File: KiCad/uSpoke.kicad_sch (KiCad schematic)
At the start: 82 parts, among them J1 B2B-PH-K-S, J12 Amphenol 132289, J2 BAT+, J3 BAT-, J5 USB+, J6 USB-, J8 PLS-1x6, J9 PLS-1x3, Q2 AO3407A, Q3 AO3400, U2 TP4056, U4 LM3671MF-3.3, U6 STM32F103C8T6, X1 8MHz

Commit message: Rename to uSpoke
(cherry picked from commit a0effae12703fde22e0195c2c61b714ac3e4bfb9)

# Conflicts:
#	KiCad/uSpoke.kicad_pcb
#	KiCad/uSpoke.kicad_sch
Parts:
- added A3: GM12864-01A, Spoke:GM12864-01A, symbol Spoke:GM12864-01A
- added A4: G10A-F30, Spoke:G10A-F30, symbol Spoke:GN-801
- added A5: TU10-F, Spoke:TU10-F, symbol Spoke:TU10-F
- added C11, C3, C30, C31, C33, C35, C6: 100nF, Spoke:C0603, symbol Spoke:C
- added C2, C32, C7: 4.7uF, Spoke:C0805, symbol Spoke:C
- added C24: 80 mF Supercap, Spoke:XH414HG-IV01E, symbol Spoke:C-Supercap
- added C28, C29: 47uF, Spoke:C_tantA, symbol Spoke:C-Polar
- added C34: 10uF, Spoke:C1206, symbol Spoke:C
- added C36: 220nF, Spoke:C0603, symbol Spoke:C
- added D3, D6: BAT54C, Spoke:SOT-23, symbol Spoke:BAT54C
- added J10: BL-A, Spoke:Pad_oval, symbol Spoke:Pad-Oval
- added J11: BL-C, Spoke:Pad_oval, symbol Spoke:Pad-Oval
- added J4: GCT USB4105/USB4110, Spoke:USB_C_16p_GCT4105, symbol Spoke:USB-TypeC-16pin
- added J7: PLS-1x3, Spoke:Header_1x3, symbol Spoke:PLS-1x3
- added LS1: Buzzer-Passive, Spoke:Buzzer, symbol Spoke:Buzzer-Passive
- added Q1: AO3407A, Spoke:SOT-23, symbol Spoke:PMOS
- added Q4, Q5, Q6: AO3400, Spoke:SOT-23, symbol Spoke:NMOS
- added R1, R3: 5.1kR, Spoke:R0603, symbol Spoke:R
- added R11, R13, R14, R37: 100kR, Spoke:R0603, symbol Spoke:R
- added R12, R29, R8: 1kR, Spoke:R0603, symbol Spoke:R
- added R18, R19, R2: 0R, Spoke:R0603, symbol Spoke:R
- added R25, R38: 300R, Spoke:R0603, symbol Spoke:R
- added R39: 100R, Spoke:R1206, symbol Spoke:R
- added R40, R41: 3.9kR, Spoke:R0603, symbol Spoke:R
- added R5: 22.1kR, Spoke:R0603, symbol Spoke:R
- added R6: 47.5kR, Spoke:R0603, symbol Spoke:R
- added SW3, SW4, SW5: ~, Spoke:Button_6x6, symbol Spoke:Button-SPST-NO
- added TP1, TP13, TP15, TP17, TP2, TP3: Pad-Round, Spoke:Pad_round, symbol Spoke:Pad-Round
- added U1: SP0503BAHTG, Spoke:SOT-143, symbol Spoke:SP0503BAHTG
- added U3: CP2102N-A02-GQFN28, Spoke:QFN-28, symbol Spoke:CP2102N-A02-GQFN28
- added U5: 74HC4052PW, Spoke:TSSOP-16, symbol Spoke:74HC4052PW
- added U7: LSM303DLHC, Spoke:LGA-14, symbol Spoke:LSM303DLHC
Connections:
- net +3V3: now also A3.2 (VCC), A4.2 (VCC), A5.4 (VCC), C11.1, C28.1, C29.1, C30.1, C31.1, C33.1, C34.2, C35.1, D3.3, D6.2, LS1.1, R29.2, R39.2, R40.2, R41.2, SW5.1, SW5.2, U5.16 (VDD), U7.1 (VDD_IO), U7.14 (VDD)
- net +BATT: now also Q1.3 (D), R2.1; no longer Q2.2 (S), R7.1
- net BLE_RXD: now also U5.12 (1Y0)
- net BLE_TXD: now also U5.1 (2Y0)
- net BOOT0: now also Q4.1 (G), SW5.3 (2), SW5.4 (2); no longer J8.3
- net BTN_ALARM: now also SW4.1, SW4.2
- net BTN_ESC: now also SW3.1, SW3.2
- net BUZZER: now also R25.1
- net CONSOLE_RXD: now also R19.1, U5.3 (2Z)
- net CONSOLE_TXD: now also R18.1, U5.13 (1Z)
- net GND: now also J8.3, A3.1 (GND), A4.1 (GND), A5.12 (GND), A5.3 (GND), C11.2, C2.1, C24.2, C28.2, C29.2, C3.1, C30.2, C31.2, C32.1, C33.2, C34.1, C35.2, C6.1, C7.1, J4.A12B1 (GND), J4.A1B12 (GND), J4.S (SHIELD), J7.3, Q1.1 (G), Q4.2 (S), Q5.2 (S), Q6.2 (S), R1.2, R14.2, R3.2, R37.1, R6.2, SW3.3 (2), SW3.4 (2), SW4.3 (2), SW4.4 (2), U1.1 (A), U3.29 (GND), U3.3 (GND), U5.6 (~{E}), U5.7 (VEE), U5.8 (GND), U7.10 (RES_(GND)), U7.11 (RES_(GND)), U7.7 (GND)
- net GPS_PPS: now also A4.5 (PPS), A5.6 (PPS)
- net GPS_RXD: now also A4.4 (RXD), A5.1 (RXD), U5.11 (1Y3)
- net GPS_TXD: now also A4.3 (TXD), A5.2 (TXD), U5.4 (2Y3)
- net I2C_INT: now also TP17.1, U7.5 (INT1)
- net I2C_SCL: now also R40.1, TP13.1, U7.2 (SCL)
- net I2C_SDA: now also R41.1, TP15.1, U7.3 (SDA)
- net LCD_BL: now also A3.8 (BL), Q6.1 (G), R37.2
- net LCD_CS: now also A3.7 (CS)
- net LCD_DC: now also A3.5 (DC)
- net LCD_MOSI: now also A3.4 (SDA)
- net LCD_RESET: now also A3.6 (RST)
- net LCD_SCK: now also A3.3 (SCL)
- net MUX_BLE_USB: now also R13.2, TP2.1, U5.10 (S0)
- net PPS_BOOT1: now also Q4.3 (D)
- net VBUS: now also C2.2, C3.2, J4.A4B9 (VBUS), J4.A9B4 (VBUS), R5.1, U1.4 (K), U3.7 (VREGIN)
- new net: Q1.2 (S), Q2.2 (S), R2.2, R7.1
- new net: D3.1, D3.2, LS1.2, Q5.3 (D), R29.1
- new net: J4.B5 (CC2), R1.1
- new net: C36.1, U7.13 (SETC)
- new net: C36.2, U7.12 (SETP)
- new net: J10.1, R39.1
- new net: R14.1, TP3.1, U5.9 (S1)
- new net: Q5.1 (G), R25.2
- new net: J11.1, Q6.3 (D)
- new net: R8.1, U3.9 (~{RST})
- new net: C32.2, U7.6 (C1)
- new net: J4.A5 (CC1), R3.1
- new net: R12.1, U3.26 (TXD)
- new net: R5.2, R6.1, U3.8 (VBUS)
- new net: D6.3, R38.2
- new net GPS_VBKP: A5.5 (VBKP), C24.1, R38.1
- new net USB_DN: J4.A7 (D-), J4.B7 (D-), U1.3 (K), U3.5 (D-)
- new net USB_DP: J4.A6 (D+), J4.B6 (D+), U1.2 (K), U3.4 (D+)
- new net USB_RXD: J7.2, R11.1, R18.2, U3.25 (RXD), U5.14 (1Y1)
- new net USB_TXD: J7.1, R12.2, R19.2, U5.5 (2Y1)
- new net VDD: C6.2, C7.2, R11.2, R13.1, R8.2, TP1.1, U3.6 (VDD)
- no-connect marks 3 -> 38
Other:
- moved on the sheet: C1, C5, D2, J5, J6, R10, R4, U2

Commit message: Remove not needed
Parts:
- removed A3: GM12864-01A, Spoke:GM12864-01A, symbol Spoke:GM12864-01A
- removed A5: TU10-F, Spoke:TU10-F, symbol Spoke:TU10-F
- removed C10, C21, C3, C31, C33, C35, C4, C6: 100nF, Spoke:C0603, symbol Spoke:C
- removed C12, C9: ~, Spoke:C0603, symbol Spoke:C
- removed C2, C32, C7: 4.7uF, Spoke:C0805, symbol Spoke:C
- removed C24: 80 mF Supercap, Spoke:XH414HG-IV01E, symbol Spoke:C-Supercap
- removed C29: 47uF, Spoke:C_tantA, symbol Spoke:C-Polar
- removed C34: 10uF, Spoke:C1206, symbol Spoke:C
- removed C36: 220nF, Spoke:C0603, symbol Spoke:C
- removed D6: BAT54C, Spoke:SOT-23, symbol Spoke:BAT54C
- removed J10: BL-A, Spoke:Pad_oval, symbol Spoke:Pad-Oval
- removed J11: BL-C, Spoke:Pad_oval, symbol Spoke:Pad-Oval
- removed J2: BAT+, Spoke:Pad_oval, symbol Spoke:Pad-Oval
- removed J3: BAT-, Spoke:Pad_oval, symbol Spoke:Pad-Oval
- removed J4: GCT USB4105/USB4110, Spoke:USB_C_16p_GCT4105, symbol Spoke:USB-TypeC-16pin
- removed J7: PLS-1x3, Spoke:Header_1x3, symbol Spoke:PLS-1x3
- removed J8: PLS-1x6, Spoke:Header_1x6, symbol Spoke:PLS-1x6
- removed Q1: AO3407A, Spoke:SOT-23, symbol Spoke:PMOS
- removed Q6: AO3400, Spoke:SOT-23, symbol Spoke:NMOS
- removed R11, R14, R30, R37: 100kR, Spoke:R0603, symbol Spoke:R
- removed R12, R22, R24, R31, R8: 1kR, Spoke:R0603, symbol Spoke:R
- removed R16: ~, Spoke:R0603, symbol Spoke:R
- removed R18, R19, R20, R35, R36: 0R, Spoke:R0603, symbol Spoke:R
- removed R38: 300R, Spoke:R0603, symbol Spoke:R
- removed R39: 100R, Spoke:R1206, symbol Spoke:R
- removed R40, R41: 3.9kR, Spoke:R0603, symbol Spoke:R
- removed R6: 47.5kR, Spoke:R0603, symbol Spoke:R
- removed SW4: ~, Spoke:Button_6x6, symbol Spoke:Button-SPST-NO
- removed TP1, TP12, TP13, TP14, TP15, TP16, TP17, TP18, TP3, TP4, TP5, TP6, TP7, TP8, TP9: Pad-Round, Spoke:Pad_round, symbol Spoke:Pad-Round
- removed U1: SP0503BAHTG, Spoke:SOT-143, symbol Spoke:SP0503BAHTG
- removed U3: CP2102N-A02-GQFN28, Spoke:QFN-28, symbol Spoke:CP2102N-A02-GQFN28
- removed U7: LSM303DLHC, Spoke:LGA-14, symbol Spoke:LSM303DLHC
- added J2, J4: PLS-1x3, Spoke:Header_1x3, symbol Spoke:PLS-1x3
- added U1: SP0503BAHTG, symbol uSpoke:SP0503BAHTG
- J5: value USB+ -> EXT
- J6: value USB- -> GND
- R1: value 5.1kR -> 100kR
- R2: value 0R -> 100kR; now fitted
- R3: value 5.1kR -> 0R; now not fitted
- R5: value 22.1kR -> 0R; now not fitted
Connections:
- net BTN_ALARM is gone; now on net BLE_MODE: U6.4 (PC15)
- net USB_TXD is gone; now on net EXT_TXD: U5.5 (2Y1)
- net VDD is gone; now on net +3V3: R13.1
- net +3V3: now also R2.1, U4.4 (FB)
- net +BATT: now also Q2.2 (S), R7.1; no longer R2.1
- net BLE_TXD: now also A1.12 (TXD)
- net CONSOLE_RXD: now also R5.1
- net CONSOLE_TXD: now also R3.1, U6.30 (PA9)
- net GND: now also A1.7 (WAKEUP/SLEEP), U5.9 (S1), J2.3, J4.3; no longer R1.2, R3.2
- net GPS_RXD: no longer U5.11 (1Y3)
- net GPS_TXD: no longer U5.4 (2Y3)
- net SWD_CLK: now also J4.1
- net SWD_IO: now also J4.2
- net at R1.1: now also Q5.1 (G), R25.2
- net BLE_MODE: now reaches A1.9 (MODE)
- net EXT_TXD: now reaches R5.2
- net EXT_TXD: now also J2.1
- net LCD_BL: no longer names the net of U6.11 (PA1)
- net LCD_CS: no longer names the net of U6.25 (PB12)
- net LCD_DC: no longer names the net of U6.29 (PA8)
- net LCD_MOSI: no longer names the net of U6.28 (PB15)
- net LCD_RESET: no longer names the net of U6.27 (PB14)
- net LCD_SCK: no longer names the net of U6.26 (PB13)
- net MUX_BLE_USB renamed MUX_BLE_EXT
- net USB_RXD renamed EXT_RXD
- net EXT_RXD: now also R2.2, R3.2, J2.2
- net VBUS renamed VEXT
- net VEXT: no longer R5.1
- no-connect marks 38 -> 6

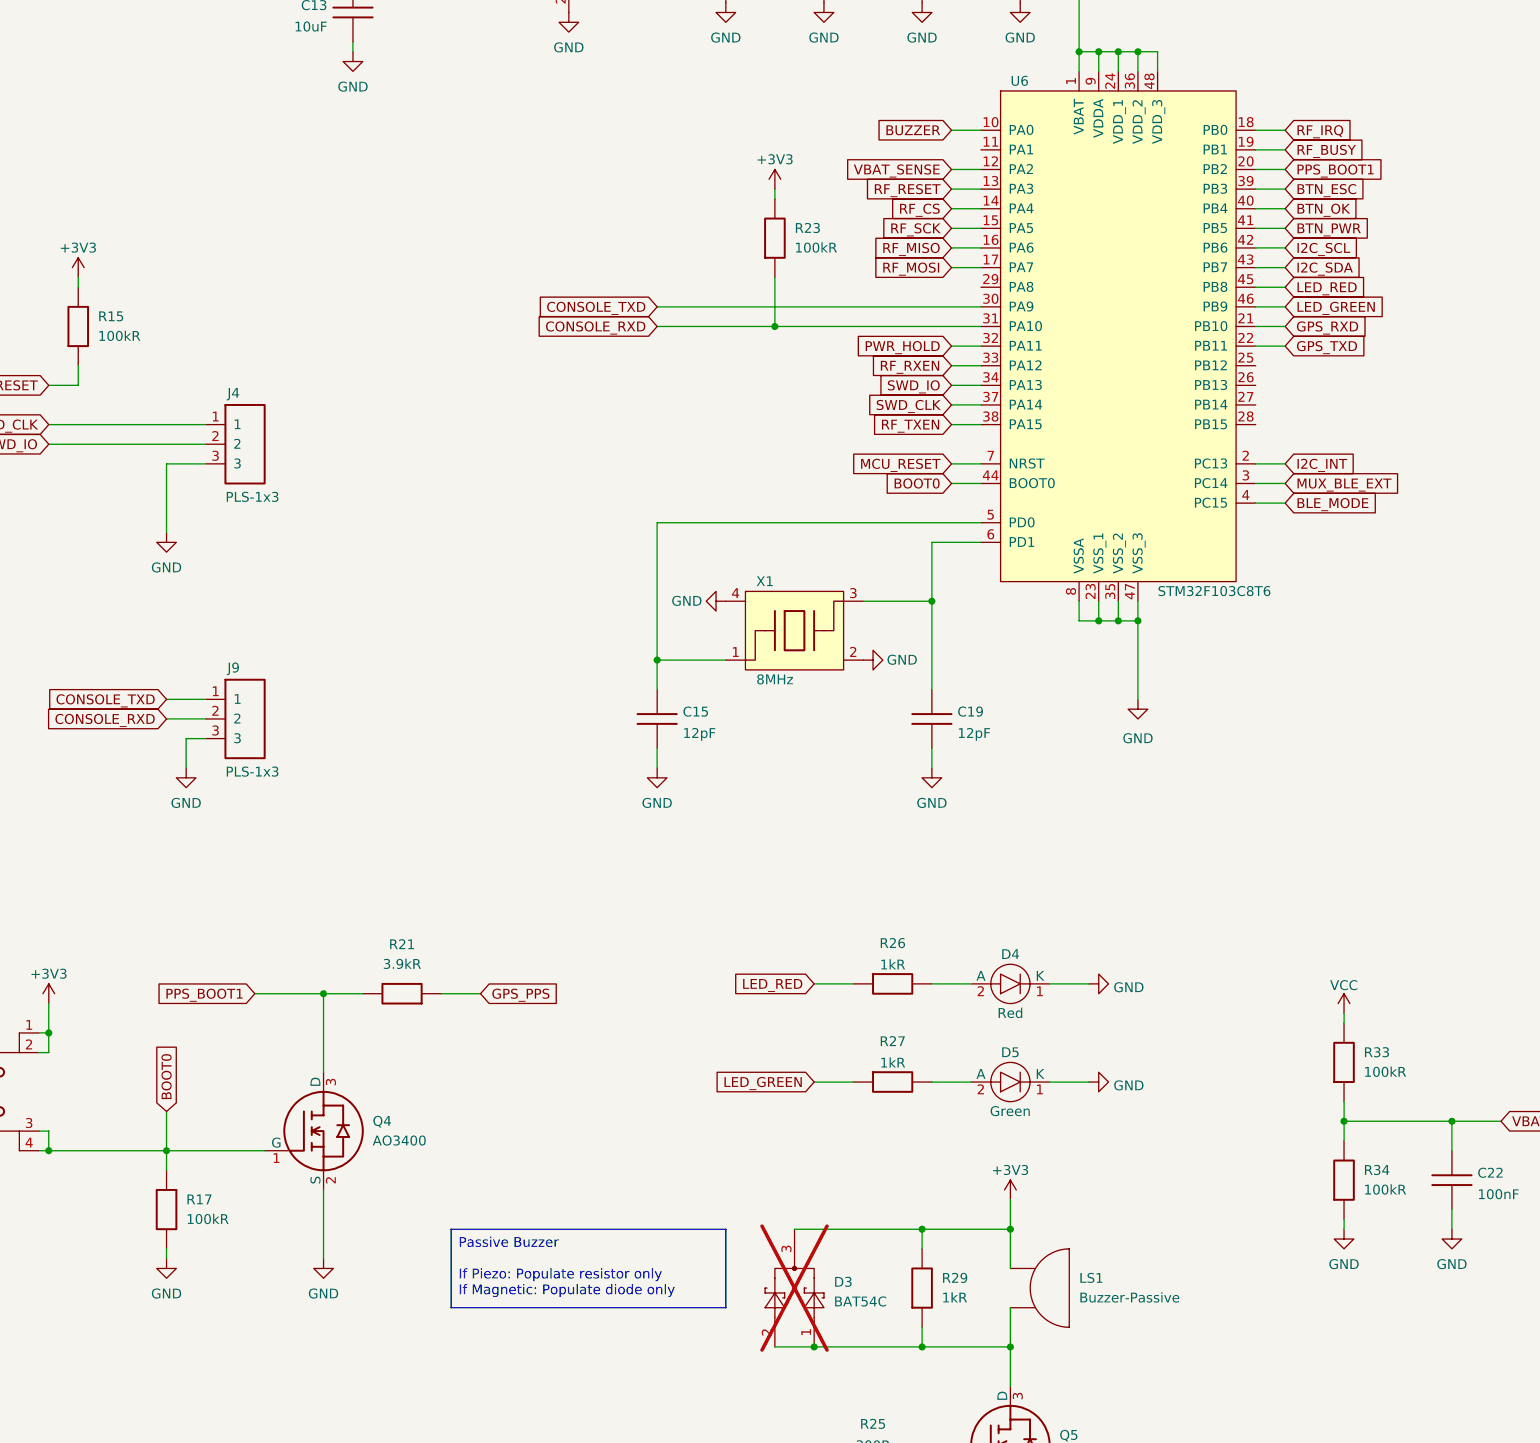
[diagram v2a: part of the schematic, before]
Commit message: Remap GPS PPS and also (earlier) map BLE_MODE in place of ALARM_BTN
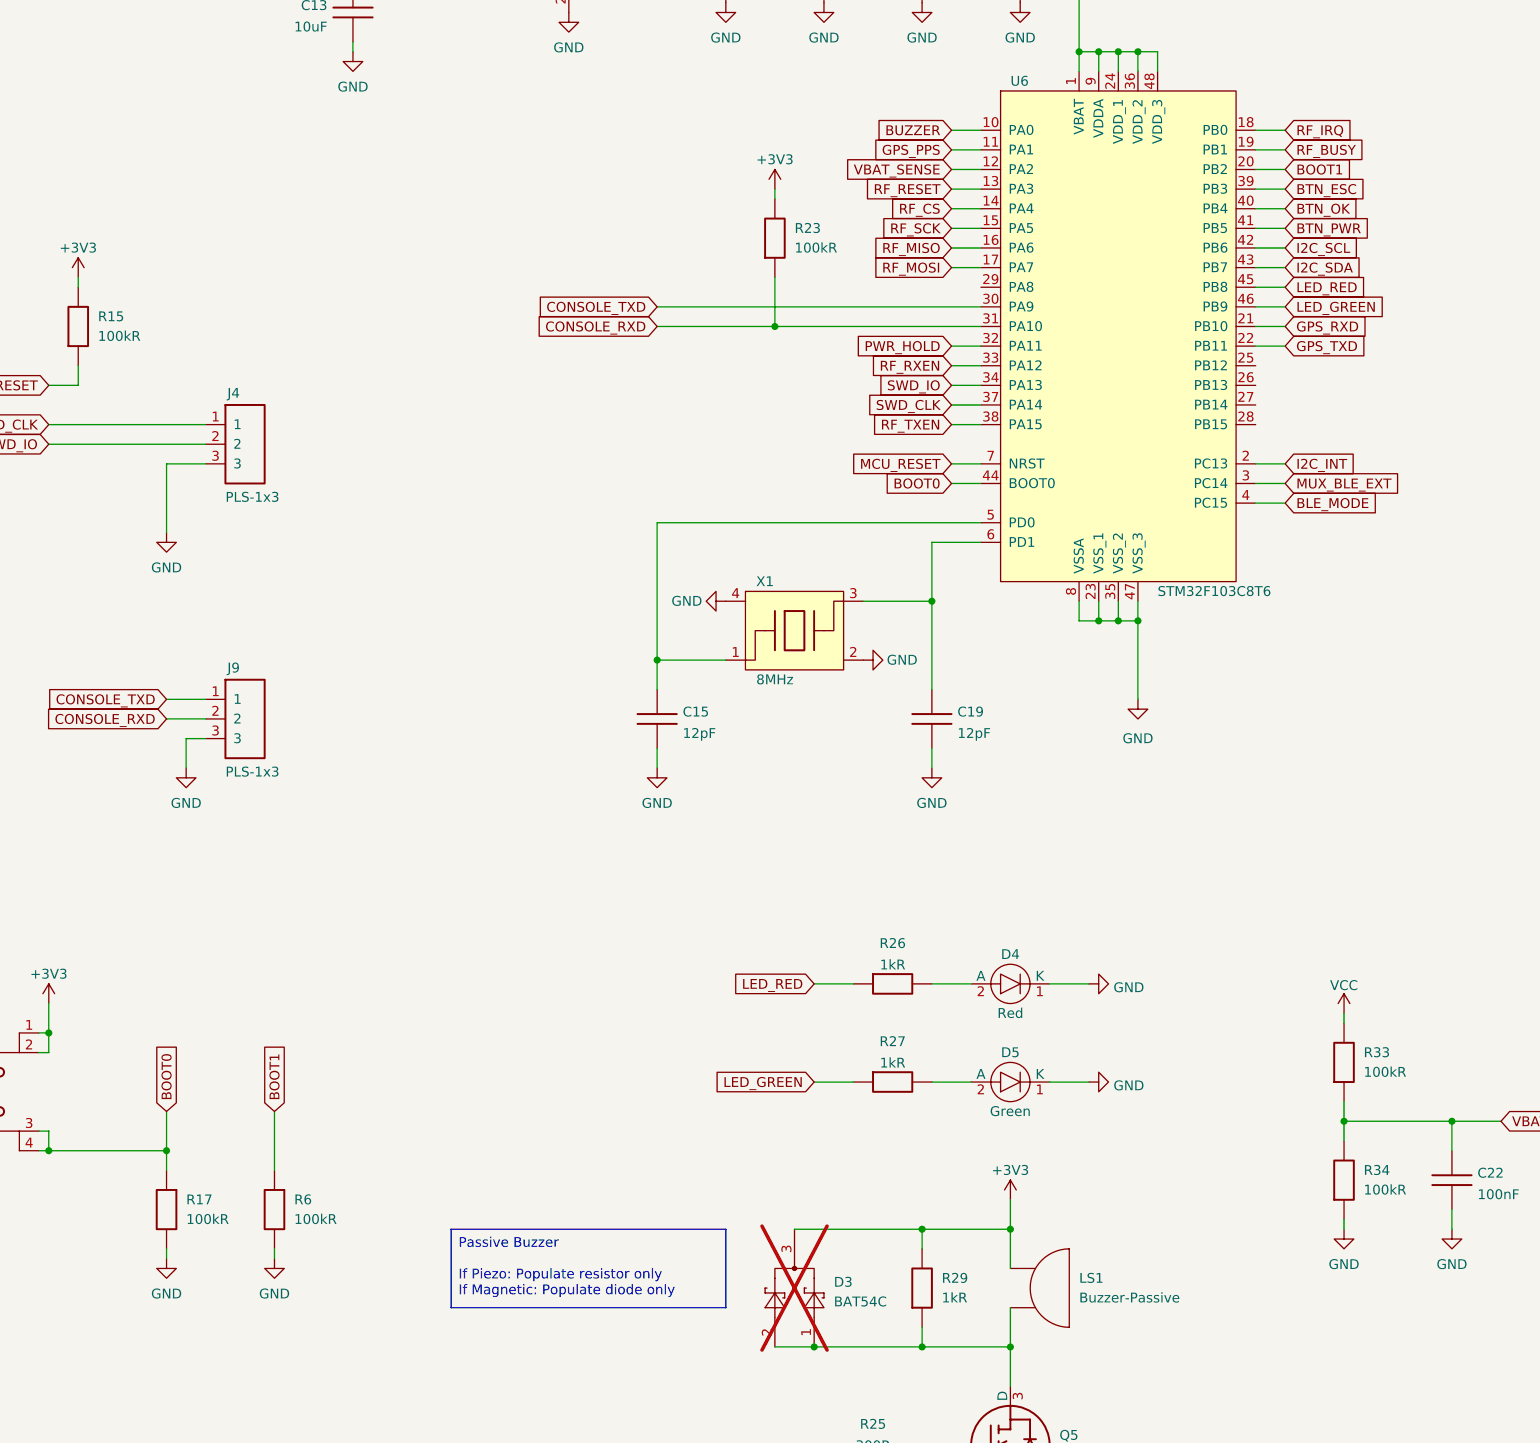
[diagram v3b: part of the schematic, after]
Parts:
- removed Q4: AO3400, Spoke:SOT-23, symbol Spoke:NMOS
- removed R21: 3.9kR, Spoke:R0603, symbol Spoke:R
- added R6: 100kR, Spoke:R0603, symbol Spoke:R
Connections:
- net GND: now also R6.2
- net GPS_PPS: now also U6.11 (PA1)
- net PPS_BOOT1 renamed BOOT1
- net BOOT1: now also R6.1

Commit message: Draft PCB
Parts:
- removed A4: G10A-F30, Spoke:G10A-F30, symbol Spoke:GN-801
- added J10, J11, J13, J14, J3, J7, J8: EXT, Spoke:Pad_oval, symbol Spoke:Pad-Oval
- U1: footprint (none) -> Spoke:SOT-23-5
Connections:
- net +3V3: now also J7.1
- net EXT_RXD: now also U1.3 (K), J14.1
- net EXT_TXD: now also U1.2 (K), J13.1
- net GND: now also R1.2, U1.1 (A), J3.1
- net GPS_PPS: now also J11.1
- net GPS_RXD: now also J10.1
- net GPS_TXD: now also J8.1
- net VEXT: now also U1.4 (K)
- net I2C_INT: no longer names the net of U6.2 (PC13)
- net I2C_SCL: no longer names the net of U6.42 (PB6)
- net I2C_SDA: no longer names the net of U6.43 (PB7)
- no-connect marks 6 -> 5
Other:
- title: LRNS SPOKE -> LRNS uSPOKE
- moved on the sheet: U1

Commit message: Some progress
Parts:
- added J15: EXT, Spoke:Pad_oval, symbol Spoke:Pad-Oval
- added R11, R8: 0R, Spoke:R0603, symbol Spoke:R
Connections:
- net BLE_RXD: now also R8.2
- net BLE_TXD: now also R11.2
- net CONSOLE_RXD: now also R11.1
- net CONSOLE_TXD: now also R8.1
- net at U6.2 (PC13): now also J15.1
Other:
- note added: "S2B-PH-SM4-TB"
- note added: "TL3330AF260QG"

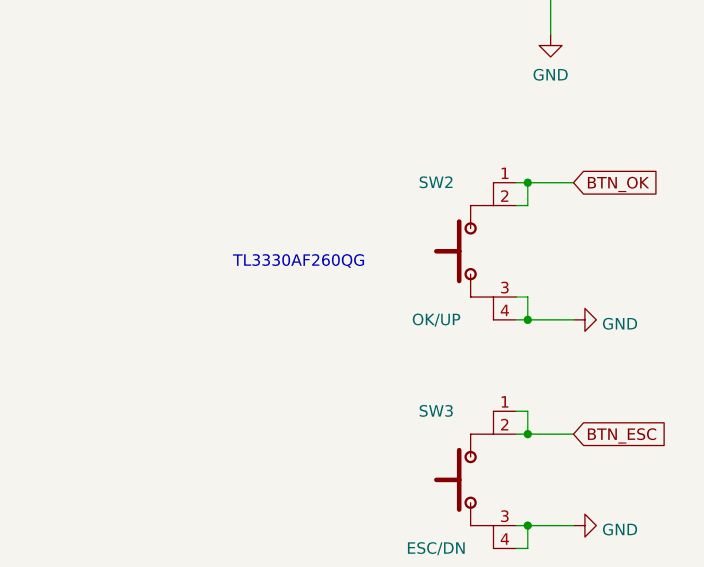
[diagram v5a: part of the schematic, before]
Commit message: Some PCB planning
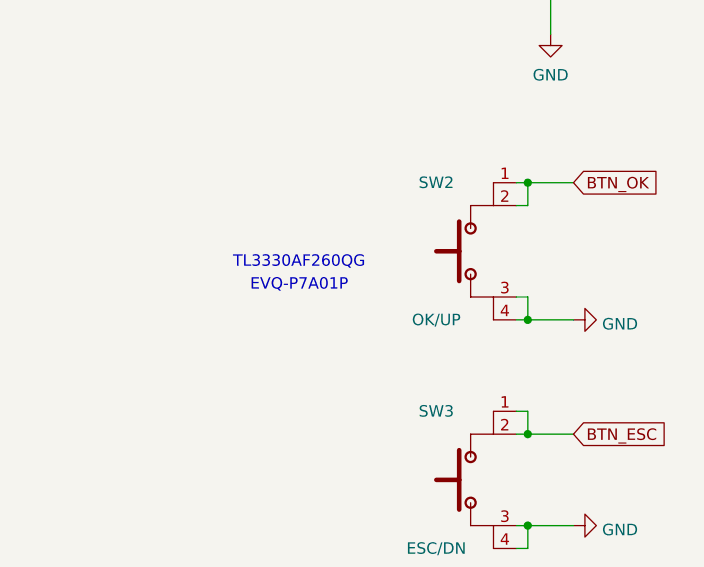
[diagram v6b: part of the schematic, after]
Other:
- note added: "EVQ-P7A01P"
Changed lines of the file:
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@@
+		)
+	)
+	(text "EVQ-P7A01P"
+		(exclude_from_sim no)
+		(at 57.15 132.08 0)
+		(effects
+			(font
+				(size 1.27 1.27)
+			)
 		)
 	)

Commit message: Clean up SCH
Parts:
- removed H1, H2, H3, H4: MountingHole, MountingHole:MountingHole_3.2mm_M3, symbol Mechanical:MountingHole
- removed J1: B2B-PH-K-S, Spoke:B2B-PH-2.0, symbol Spoke:B2B-PH-K-S
- removed J10, J11, J13, J14, J15, J3, J5, J7, J8: EXT, Spoke:Pad_oval, symbol Spoke:Pad-Oval
- removed J6: GND, Spoke:Pad_oval, symbol Spoke:Pad-Oval
- removed J9: PLS-1x3, Spoke:Header_1x3, symbol Spoke:PLS-1x3
- removed LS1: Buzzer-Passive, Spoke:Buzzer, symbol Spoke:Buzzer-Passive
- removed R2: 100kR, Spoke:R0603, symbol Spoke:R
- removed R25: 300R, Spoke:R0603, symbol Spoke:R
- removed TP2: Pad-Round, Spoke:Pad_round, symbol Spoke:Pad-Round
- added R12: 1kR, Spoke:R0603, symbol Spoke:R
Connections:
- net BUZZER: now also R12.1
- net BUZZ_N: now reaches D3.1, D3.2, Q5.3 (D), R29.1
- net at Q5.1 (G), R1.1: now also R12.2
- net MOVE_SW: now reaches U6.2 (PC13)
- net EXT_RXD renamed CONSOLE_RXD_EXT
- net CONSOLE_RXD_EXT: now also R5.2, U5.5 (2Y1); no longer R3.2, U5.14 (1Y1)
- net EXT_TXD renamed CONSOLE_TXD_EXT
- net CONSOLE_TXD_EXT: now also R3.2, U5.14 (1Y1); no longer R5.2, U5.5 (2Y1)
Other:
- note added: "BAT V+ BAT V+ BAT GND BAT GND GPS TX GPS RX GPS PPS GPS V+ GPS GND BUZZ+ BUZZ- I2C SCK I2C SDA I2C GND MOVE SW+ MOVE SW- SWDIO SWCLK GND"
- note added: "BAT V+ BAT V+ BAT GND BAT GND GPS TX GPS RX GPS PPS GPS V+ GPS GND BUZZ+ BUZZ- MOVE+"
- note added: "I2C SCK I2C SDA I2C GND SWDIO SWCLK GND"
- note added: "MCP73831T"
- note added: "SM12B-SRSS-TB"
- moved on the sheet: C28, C30
